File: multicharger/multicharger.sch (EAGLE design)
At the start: 24 parts, among them J2 USB-MICROA-AMPHENOL-10118192-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, J3 HEADER-8POS-, P1 TEST-POINT, P2 TEST-POINT, P3 TEST-POINT, P4 TEST-POINT, P5 TEST-POINT, P6 TEST-POINT, U1 MCP73831T-2ACI/OT, U2 MCP73831T-2ACI/OT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

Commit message: smaller LEDs for multi-charger
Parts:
- D1, D2, D3, D4: value LED-2X-GREEN/RED -> LED-2X-GREEN/RED-1.6X1.5MM; device RemoteParts:LED-2X-GREEN/RED -> RemoteParts:LED-2X-GREEN/RED-1.6X1.5MM
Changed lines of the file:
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@@
 <setting verticaltext="up"/>
 </settings>
-<grid distance="0.05" unitdist="inch" unit="inch" style="lines" multiple="1" display="no" altdistance="0.01" altunitdist="inch" altunit="inch"/>
+<grid distance="0.1" unitdist="inch" unit="inch" style="lines" multiple="1" display="no" altdistance="0.01" altunitdist="inch" altunit="inch"/>
 <layers>
 <layer number="1" name="Top" color="4" fill="1" visible="no" active="no"/>
@@
 <part name="C6" library="quadparts_prebuilt" deviceset="CAPACITOR-NP_" device="SMD-0603_CERAMIC-10UF" package3d_urn="urn:adsk.eagle:package:11135716/1" value="10uF"/>
 <part name="P+23" library="quadparts_prebuilt" deviceset="GND" device=""/>
-<part name="D1" library="RemoteParts" deviceset="LED-2X" device="-GREEN/RED"/>
+<part name="D1" library="RemoteParts" deviceset="LED-2X" device="-GREEN/RED-1.6X1.5MM" value="LED-2X-GREEN/RED-1.6X1.5MM"/>
 <part name="R2" library="quadparts_prebuilt" deviceset="RESISTOR-PACK-4X" device="-510" package3d_urn="urn:adsk.eagle:package:10895048/1" value="510"/>
 <part name="U2" library="RemoteParts" deviceset="MCP73831/2" device="" value="MCP73831T-2ACI/OT"/>
@@
 <part name="C2" library="quadparts_prebuilt" deviceset="CAPACITOR-NP_" device="SMD-0603_CERAMIC-10UF" package3d_urn="urn:adsk.eagle:package:11135716/1" value="10uF"/>
 <part name="P+5" library="quadparts_prebuilt" deviceset="GND" device=""/>
-<part name="D2" library="RemoteParts" deviceset="LED-2X" device="-GREEN/RED"/>
+<part name="D2" library="RemoteParts" deviceset="LED-2X" device="-GREEN/RED-1.6X1.5MM" value="LED-2X-GREEN/RED-1.6X1.5MM"/>
 <part name="U3" library="RemoteParts" deviceset="MCP73831/2" device="" value="MCP73831T-2ACI/OT"/>
 <part name="P+7" library="quadparts_prebuilt" deviceset="GND" device=""/>
@@
 <part name="C4" library="quadparts_prebuilt" deviceset="CAPACITOR-NP_" device="SMD-0603_CERAMIC-10UF" package3d_urn="urn:adsk.eagle:package:11135716/1" value="10uF"/>
 <part name="P+10" library="quadparts_prebuilt" deviceset="GND" device=""/>
-<part name="D3" library="RemoteParts" deviceset="LED-2X" device="-GREEN/RED"/>
+<part name="D3" library="RemoteParts" deviceset="LED-2X" device="-GREEN/RED-1.6X1.5MM" value="LED-2X-GREEN/RED-1.6X1.5MM"/>
 <part name="U4" library="RemoteParts" deviceset="MCP73831/2" device="" value="MCP73831T-2ACI/OT"/>
 <part name="P+12" library="quadparts_prebuilt" deviceset="GND" device=""/>
@@
 <part name="C8" library="quadparts_prebuilt" deviceset="CAPACITOR-NP_" device="SMD-0603_CERAMIC-10UF" package3d_urn="urn:adsk.eagle:package:11135716/1" value="10uF"/>
 <part name="P+15" library="quadparts_prebuilt" deviceset="GND" device=""/>
-<part name="D4" library="RemoteParts" deviceset="LED-2X" device="-GREEN/RED"/>
+<part name="D4" library="RemoteParts" deviceset="LED-2X" device="-GREEN/RED-1.6X1.5MM" value="LED-2X-GREEN/RED-1.6X1.5MM"/>
 <part name="R3" library="quadparts_prebuilt" deviceset="RESISTOR-PACK-4X" device="-510" package3d_urn="urn:adsk.eagle:package:10895048/1" value="510"/>
 <part name="R5" library="quadparts_prebuilt" deviceset="RESISTOR-PACK-4X" device="-2K" package3d_urn="urn:adsk.eagle:package:10895048/1" value="2K"/>

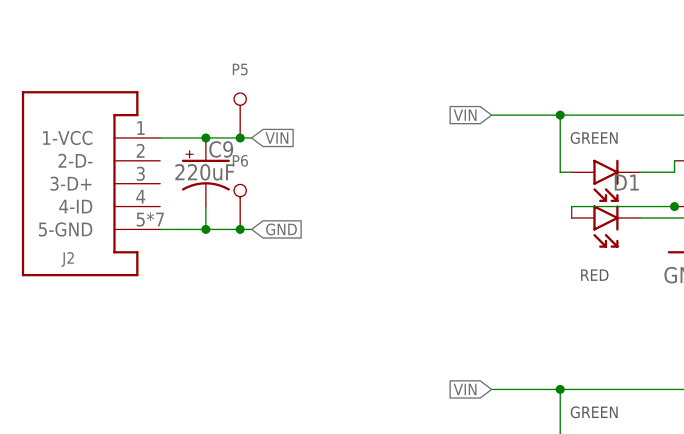
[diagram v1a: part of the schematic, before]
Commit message: make file, better-looking layout
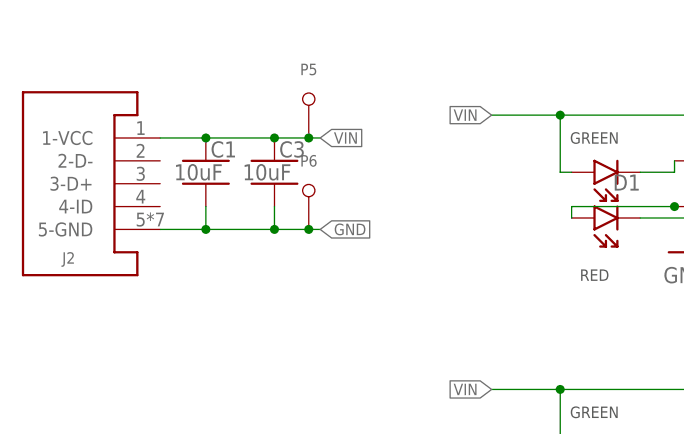
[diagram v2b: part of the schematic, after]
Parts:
- removed C9: 220uF, quadparts_prebuilt:CAPACITOR-POL_SMD-7043-D_TANTALUM-220UF
- added C1, C3: 10uF, quadparts_prebuilt:CAPACITOR-NP_SMD-0603_CERAMIC-10UF
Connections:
- net GND: now also C1.2, C3.2; no longer C9.-
- net VIN: now also C1.1, C3.1; no longer C9.+
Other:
- moved on the sheet: P5, P6
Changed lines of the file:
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@@
 <part name="P5" library="RemoteParts" deviceset="TEST-POINT" device=""/>
 <part name="P6" library="RemoteParts" deviceset="TEST-POINT" device=""/>
-<part name="C9" library="quadparts_prebuilt" deviceset="CAPACITOR-POL_" device="SMD-7043-D_TANTALUM-220UF" value="220uF"/>
+<part name="C1" library="quadparts_prebuilt" deviceset="CAPACITOR-NP_" device="SMD-0603_CERAMIC-10UF" package3d_urn="urn:adsk.eagle:package:11135716/1" value="10uF"/>
+<part name="C3" library="quadparts_prebuilt" deviceset="CAPACITOR-NP_" device="SMD-0603_CERAMIC-10UF" package3d_urn="urn:adsk.eagle:package:11135716/1" value="10uF"/>
 </parts>
 <sheets>
@@
 <attribute name="NAME" x="243.84" y="102.87" size="1.27" layer="95" align="center"/>
 </instance>
-<instance part="P5" gate="G$1" x="120.65" y="185.42" smashed="yes">
-<attribute name="NAME" x="120.65" y="193.04" size="1.27" layer="95" align="center"/>
-</instance>
-<instance part="P6" gate="G$1" x="120.65" y="175.26" smashed="yes">
-<attribute name="NAME" x="120.65" y="182.88" size="1.27" layer="95" align="center"/>
-</instance>
-<instance part="C9" gate="G$1" x="116.84" y="182.88" smashed="yes">
+<instance part="P5" gate="G$1" x="128.27" y="185.42" smashed="yes">
+<attribute name="NAME" x="128.27" y="193.04" size="1.27" layer="95" align="center"/>
+</instance>
+<instance part="P6" gate="G$1" x="128.27" y="175.26" smashed="yes">
+<attribute name="NAME" x="128.27" y="182.88" size="1.27" layer="95" align="center"/>
+</instance>
+<instance part="C1" gate="G$1" x="116.84" y="182.88" smashed="yes">
 <attribute name="VALUE" x="113.284" y="180.721" size="1.778" layer="96"/>
-<attribute name="NAME" x="117.094" y="183.261" size="1.778" layer="95"/>
+<attribute name="NAME" x="117.348" y="183.261" size="1.778" layer="95"/>
+</instance>
+<instance part="C3" gate="G$1" x="124.46" y="182.88" smashed="yes">
+<attribute name="VALUE" x="120.904" y="180.721" size="1.778" layer="96"/>
+<attribute name="NAME" x="124.968" y="183.261" size="1.778" layer="95"/>
 </instance>
 </instances>
@@
 <pinref part="J2" gate="A" pin="5-GND"/>
 <wire x1="111.76" y1="175.26" x2="116.84" y2="175.26" width="0.1524" layer="91"/>
-<label x="121.92" y="175.26" size="1.27" layer="95" xref="yes"/>
+<label x="129.54" y="175.26" size="1.27" layer="95" xref="yes"/>
 <pinref part="P6" gate="G$1" pin="T"/>
-<wire x1="116.84" y1="175.26" x2="120.65" y2="175.26" width="0.1524" layer="91"/>
-<wire x1="120.65" y1="175.26" x2="121.92" y2="175.26" width="0.1524" layer="91"/>
-<junction x="120.65" y="175.26"/>
-<pinref part="C9" gate="G$1" pin="-"/>
+<wire x1="116.84" y1="175.26" x2="124.46" y2="175.26" width="0.1524" layer="91"/>
+<wire x1="124.46" y1="175.26" x2="128.27" y2="175.26" width="0.1524" layer="91"/>
+<wire x1="128.27" y1="175.26" x2="129.54" y2="175.26" width="0.1524" layer="91"/>
+<junction x="128.27" y="175.26"/>
+<pinref part="C1" gate="G$1" pin="2"/>
 <wire x1="116.84" y1="177.8" x2="116.84" y2="175.26" width="0.1524" layer="91"/>
 <junction x="116.84" y="175.26"/>
+<pinref part="C3" gate="G$1" pin="2"/>
+<wire x1="124.46" y1="177.8" x2="124.46" y2="175.26" width="0.1524" layer="91"/>
+<junction x="124.46" y="175.26"/>
 </segment>
 </net>
@@
 <net name="VIN" class="4">
 <segment>
-<label x="121.92" y="185.42" size="1.27" layer="95" xref="yes"/>
+<label x="129.54" y="185.42" size="1.27" layer="95" xref="yes"/>
 <pinref part="J2" gate="A" pin="1-VCC"/>
-<wire x1="121.92" y1="185.42" x2="120.65" y2="185.42" width="0.1524" layer="91"/>
+<wire x1="129.54" y1="185.42" x2="128.27" y2="185.42" width="0.1524" layer="91"/>
 <pinref part="P5" gate="G$1" pin="T"/>
-<wire x1="120.65" y1="185.42" x2="116.84" y2="185.42" width="0.1524" layer="91"/>
-<junction x="120.65" y="185.42"/>
-<pinref part="C9" gate="G$1" pin="+"/>
+<junction x="128.27" y="185.42"/>
+<wire x1="128.27" y1="185.42" x2="124.46" y2="185.42" width="0.1524" layer="91"/>
+<pinref part="C3" gate="G$1" pin="1"/>
+<wire x1="124.46" y1="185.42" x2="116.84" y2="185.42" width="0.1524" layer="91"/>
+<junction x="124.46" y="185.42"/>
+<pinref part="C1" gate="G$1" pin="1"/>
 <wire x1="116.84" y1="185.42" x2="111.76" y2="185.42" width="0.1524" layer="91"/>
 <junction x="116.84" y="185.42"/>

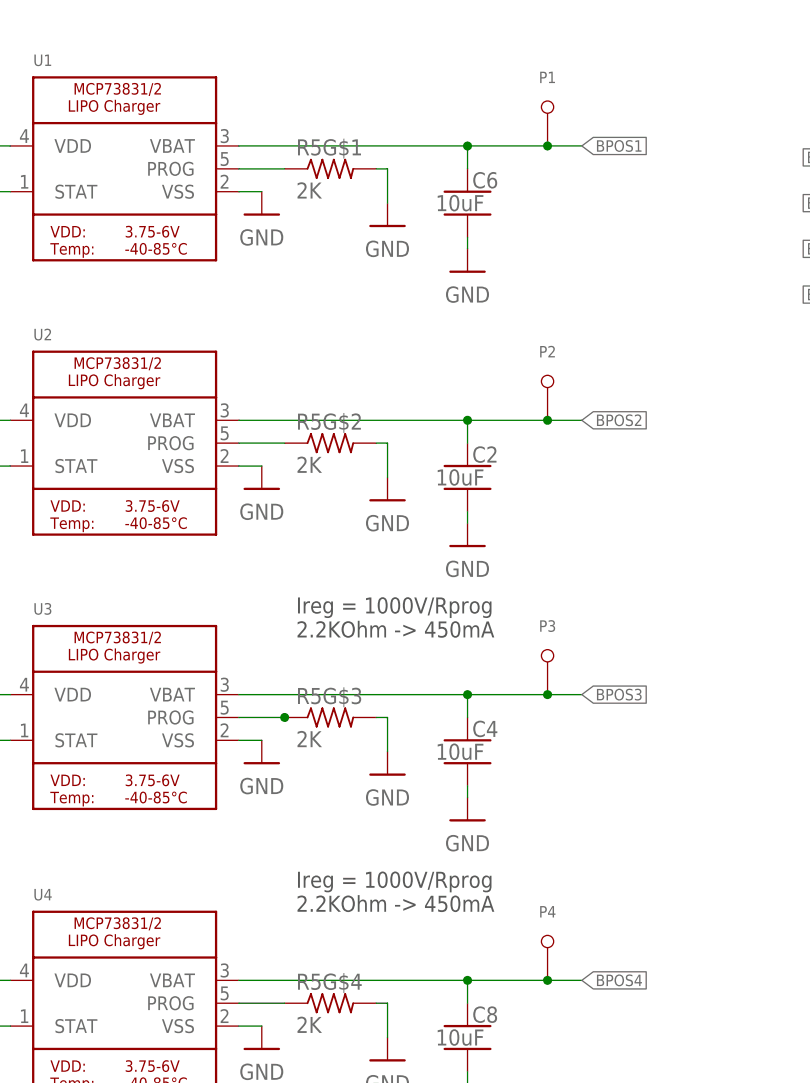
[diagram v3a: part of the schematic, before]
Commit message: cosmetic changes to schematic
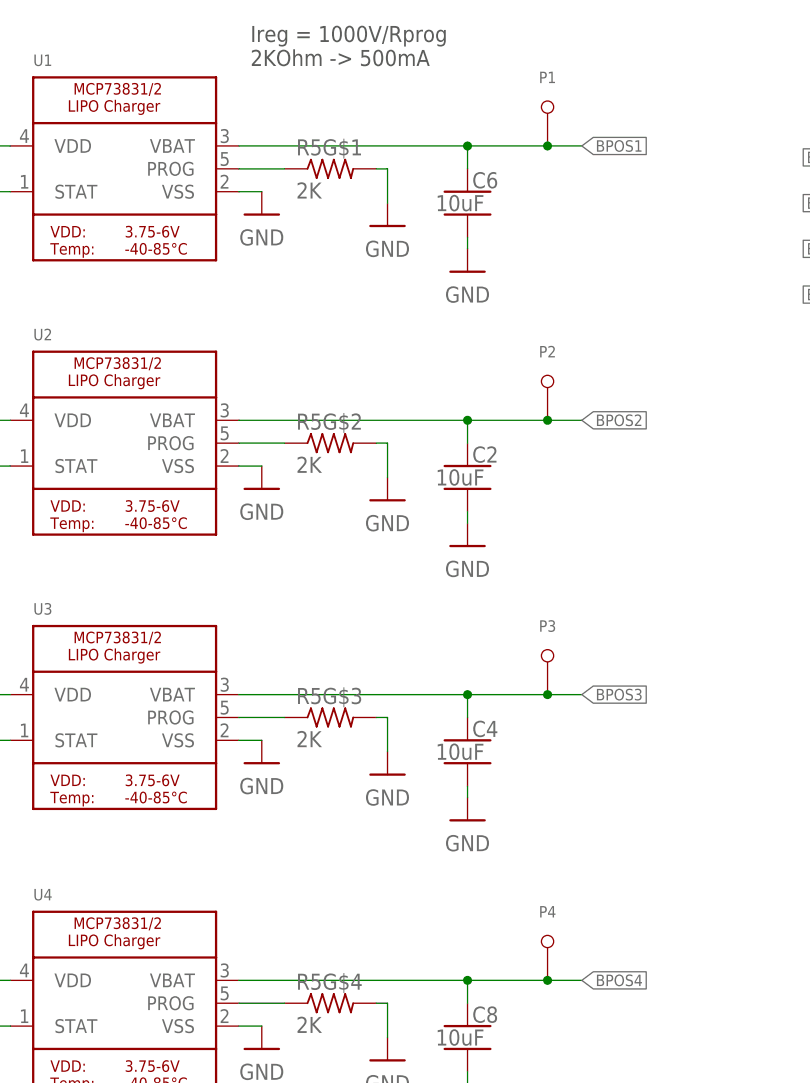
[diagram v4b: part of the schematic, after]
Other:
- note added: "Ireg = 1000V/Rprog 2KOhm -> 500mA"
- note removed: "Ireg = 1000V/Rprog 2.2KOhm -> 450mA"
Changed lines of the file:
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@@
 <sheet>
 <plain>
-<text x="215.9" y="133.35" size="1.778" layer="97">Ireg = 1000V/Rprog
-2.2KOhm -&gt; 450mA</text>
-<text x="215.9" y="102.87" size="1.778" layer="97">Ireg = 1000V/Rprog
-2.2KOhm -&gt; 450mA</text>
+<text x="210.82" y="196.85" size="1.778" layer="97">Ireg = 1000V/Rprog
+2KOhm -&gt; 500mA</text>
 </plain>
 <instances>
@@
 <wire x1="209.55" y1="124.46" x2="214.63" y2="124.46" width="0.1524" layer="91"/>
 <pinref part="R5" gate="G$3" pin="1"/>
-<junction x="214.63" y="124.46"/>
-</segment>
-</net>
+</segment>
+</net>

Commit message: Bigger resistors on leds
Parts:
- added P7: 10K, RemoteParts:TRIMPOT-BOT-ADJUST
- added P8, P9: TEST-POINT-1MM, RemoteParts:TEST-POINT-1MM
- J2: value USB-MICROA-AMPHENOL-10118192-0001LF -> USB-A-SMD-KEYSTONE-931; device RemoteParts:USB-MICROA-AMPHENOL-10118192-0001LF -> RemoteParts:USB-A-SMD-KEYSTONE-931
- P1, P2, P3, P4, P5, P6: value TEST-POINT -> TEST-POINT-1MM; device RemoteParts:TEST-POINT -> RemoteParts:TEST-POINT-1MM
- R2, R3: value 510 -> 750; device quadparts_prebuilt:RESISTOR-PACK-4X-510 -> quadparts_prebuilt:RESISTOR-PACK-4X-750
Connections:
- new net N$17: P7.A, P8.T
- new net N$18: P7.E, P9.T
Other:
- note added: "Ireg = 1000V/Rprog 2.2KOhm -> 450mA"
- note added: "leds are unbalanced. When they are both on green is too bright."
- note added: "test wether we can use the pot"
- note removed: "Ireg = 1000V/Rprog 2KOhm -> 500mA"
- moved on the sheet: J2
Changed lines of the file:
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@@
 <part name="P+23" library="quadparts_prebuilt" deviceset="GND" device=""/>
 <part name="D1" library="RemoteParts" deviceset="LED-2X" device="-GREEN/RED-1.6X1.5MM" value="LED-2X-GREEN/RED-1.6X1.5MM"/>
-<part name="R2" library="quadparts_prebuilt" deviceset="RESISTOR-PACK-4X" device="-510" package3d_urn="urn:adsk.eagle:package:10895048/1" value="510"/>
+<part name="R2" library="quadparts_prebuilt" deviceset="RESISTOR-PACK-4X" device="-750" package3d_urn="urn:adsk.eagle:package:10895048/1" value="750"/>
 <part name="U2" library="RemoteParts" deviceset="MCP73831/2" device="" value="MCP73831T-2ACI/OT"/>
 <part name="P+2" library="quadparts_prebuilt" deviceset="GND" device=""/>
@@
 <part name="P+15" library="quadparts_prebuilt" deviceset="GND" device=""/>
 <part name="D4" library="RemoteParts" deviceset="LED-2X" device="-GREEN/RED-1.6X1.5MM" value="LED-2X-GREEN/RED-1.6X1.5MM"/>
-<part name="R3" library="quadparts_prebuilt" deviceset="RESISTOR-PACK-4X" device="-510" package3d_urn="urn:adsk.eagle:package:10895048/1" value="510"/>
+<part name="R3" library="quadparts_prebuilt" deviceset="RESISTOR-PACK-4X" device="-750" package3d_urn="urn:adsk.eagle:package:10895048/1" value="750"/>
 <part name="R5" library="quadparts_prebuilt" deviceset="RESISTOR-PACK-4X" device="-2K" package3d_urn="urn:adsk.eagle:package:10895048/1" value="2K"/>
 <part name="FRAME1" library="quadparts_prebuilt" deviceset="FRAME_B_L" device=""/>
-<part name="J2" library="RemoteParts" deviceset="USB" device="-MICROA-AMPHENOL-10118192-0001LF"/>
+<part name="J2" library="RemoteParts" deviceset="USB" device="-A-SMD-KEYSTONE-931" value="USB-A-SMD-KEYSTONE-931"/>
 <part name="J3" library="quadparts_prebuilt" deviceset="HEADER-8POS-" device="">
 <attribute name="PIN1" value="-"/>
@@
 <attribute name="PIN8" value="+"/>
 </part>
-<part name="P1" library="RemoteParts" deviceset="TEST-POINT" device=""/>
-<part name="P2" library="RemoteParts" deviceset="TEST-POINT" device=""/>
-<part name="P3" library="RemoteParts" deviceset="TEST-POINT" device=""/>
-<part name="P4" library="RemoteParts" deviceset="TEST-POINT" device=""/>
-<part name="P5" library="RemoteParts" deviceset="TEST-POINT" device=""/>
-<part name="P6" library="RemoteParts" deviceset="TEST-POINT" device=""/>
+<part name="P1" library="RemoteParts" deviceset="TEST-POINT" device="-1MM" value="TEST-POINT-1MM"/>
+<part name="P2" library="RemoteParts" deviceset="TEST-POINT" device="-1MM" value="TEST-POINT-1MM"/>
+<part name="P3" library="RemoteParts" deviceset="TEST-POINT" device="-1MM" value="TEST-POINT-1MM"/>
+<part name="P4" library="RemoteParts" deviceset="TEST-POINT" device="-1MM" value="TEST-POINT-1MM"/>
+<part name="P5" library="RemoteParts" deviceset="TEST-POINT" device="-1MM" value="TEST-POINT-1MM"/>
+<part name="P6" library="RemoteParts" deviceset="TEST-POINT" device="-1MM" value="TEST-POINT-1MM"/>
 <part name="C1" library="quadparts_prebuilt" deviceset="CAPACITOR-NP_" device="SMD-0603_CERAMIC-10UF" package3d_urn="urn:adsk.eagle:package:11135716/1" value="10uF"/>
 <part name="C3" library="quadparts_prebuilt" deviceset="CAPACITOR-NP_" device="SMD-0603_CERAMIC-10UF" package3d_urn="urn:adsk.eagle:package:11135716/1" value="10uF"/>
+<part name="P7" library="RemoteParts" deviceset="TRIMPOT" device="-BOT-ADJUST" value="10K"/>
+<part name="P8" library="RemoteParts" deviceset="TEST-POINT" device="-1MM" value="TEST-POINT-1MM"/>
+<part name="P9" library="RemoteParts" deviceset="TEST-POINT" device="-1MM" value="TEST-POINT-1MM"/>
 </parts>
 <sheets>
 <sheet>
 <plain>
-<text x="210.82" y="196.85" size="1.778" layer="97">Ireg = 1000V/Rprog
-2KOhm -&gt; 500mA</text>
+<text x="215.9" y="133.35" size="1.778" layer="97">Ireg = 1000V/Rprog
+2.2KOhm -&gt; 450mA</text>
+<text x="215.9" y="102.87" size="1.778" layer="97">Ireg = 1000V/Rprog
+2.2KOhm -&gt; 450mA</text>
+<text x="99.06" y="162.56" size="1.778" layer="91">leds are unbalanced. When they are both on green is too bright.</text>
+<text x="96.52" y="152.4" size="1.778" layer="91">test wether we can use the pot</text>
 </plain>
 <instances>
@@
 <attribute name="VALUE" x="120.904" y="180.721" size="1.778" layer="96"/>
 <attribute name="NAME" x="124.968" y="183.261" size="1.778" layer="95"/>
+</instance>
+<instance part="P7" gate="G$1" x="114.3" y="139.7" smashed="yes" rot="R90">
+<attribute name="VALUE" x="118.11" y="135.89" size="1.778" layer="96" rot="R180"/>
+<attribute name="NAME" x="118.11" y="133.731" size="1.778" layer="95" rot="R180"/>
+</instance>
+<instance part="P8" gate="G$1" x="119.38" y="139.7" smashed="yes">
+<attribute name="NAME" x="119.38" y="147.32" size="1.27" layer="95" align="center"/>
+</instance>
+<instance part="P9" gate="G$1" x="109.22" y="139.7" smashed="yes">
+<attribute name="NAME" x="109.22" y="147.32" size="1.27" layer="95" align="center"/>
 </instance>
 </instances>
@@
 <wire x1="209.55" y1="124.46" x2="214.63" y2="124.46" width="0.1524" layer="91"/>
 <pinref part="R5" gate="G$3" pin="1"/>
+<junction x="214.63" y="124.46"/>
 </segment>
 </net>
@@
 </segment>
 </net>
+<net name="N$17" class="0">
+<segment>
+<pinref part="P7" gate="G$1" pin="A"/>
+<pinref part="P8" gate="G$1" pin="T"/>
+</segment>
+</net>
+<net name="N$18" class="0">
+<segment>
+<pinref part="P7" gate="G$1" pin="E"/>
+<pinref part="P9" gate="G$1" pin="T"/>
+</segment>
+</net>

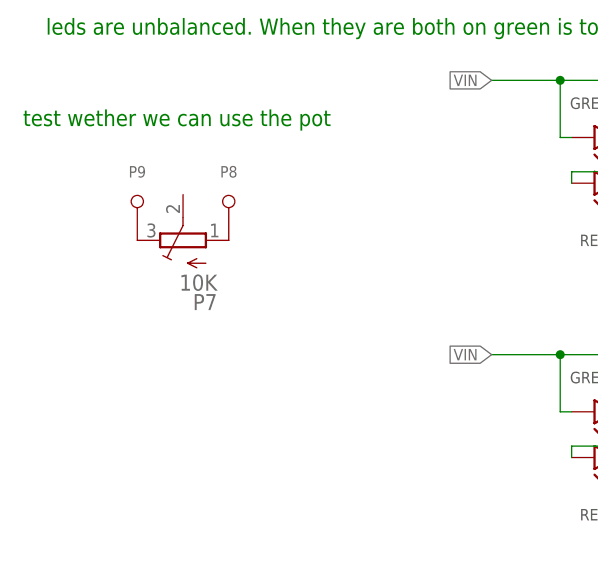
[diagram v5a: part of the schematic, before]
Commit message: tweaks to multi-charger
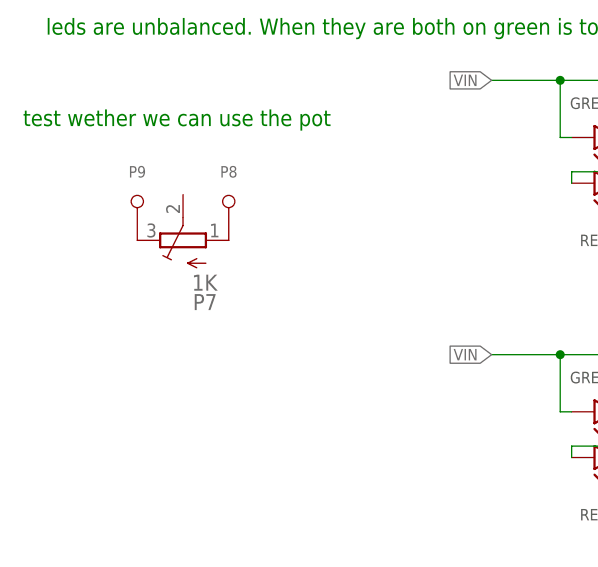
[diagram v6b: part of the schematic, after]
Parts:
- P7: value 10K -> 1K; device RemoteParts:TRIMPOT-BOT-ADJUST -> RemoteParts:TRIMPOT-BOT-ADJUST-1K
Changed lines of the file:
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@@
 <part name="C1" library="quadparts_prebuilt" deviceset="CAPACITOR-NP_" device="SMD-0603_CERAMIC-10UF" package3d_urn="urn:adsk.eagle:package:11135716/1" value="10uF"/>
 <part name="C3" library="quadparts_prebuilt" deviceset="CAPACITOR-NP_" device="SMD-0603_CERAMIC-10UF" package3d_urn="urn:adsk.eagle:package:11135716/1" value="10uF"/>
-<part name="P7" library="RemoteParts" deviceset="TRIMPOT" device="-BOT-ADJUST" value="10K"/>
+<part name="P7" library="RemoteParts" deviceset="TRIMPOT" device="-BOT-ADJUST-1K" value="1K"/>
 <part name="P8" library="RemoteParts" deviceset="TEST-POINT" device="-1MM" value="TEST-POINT-1MM"/>
 <part name="P9" library="RemoteParts" deviceset="TEST-POINT" device="-1MM" value="TEST-POINT-1MM"/>
